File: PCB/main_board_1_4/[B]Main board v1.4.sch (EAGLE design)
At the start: 117 parts, among them J1 6P_CONN, J2 RJ11MX-95001-2661, J3 POWER_JACKPTH, J4 RJ45_MX-95001-2881, J5 RJ45_MX-95001-2881, J6 RJ45_MX-95001-2881, J7 10104111-0001LF, K1 RELAY, K2 RELAY, Q1 BC807-40SMD, T3 IRLML2244, T4 2N7002PW, U4 VREG_MIC5216, U5 TPS62133RGTT, U6 CC2D23-CHIPCAP2, U7 PIC24FJ256GB206, U8 LMC555

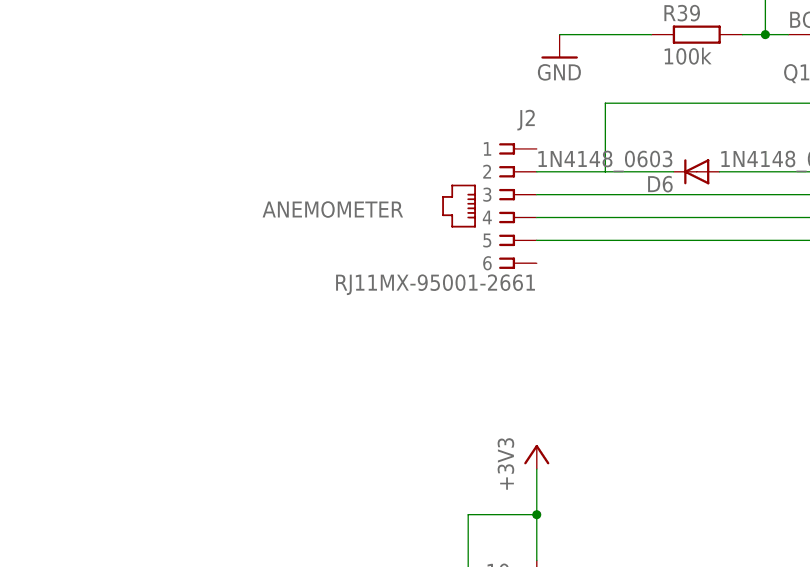
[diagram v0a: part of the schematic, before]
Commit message: Latest revision of PCB with support for RainGauge and some other sensors.
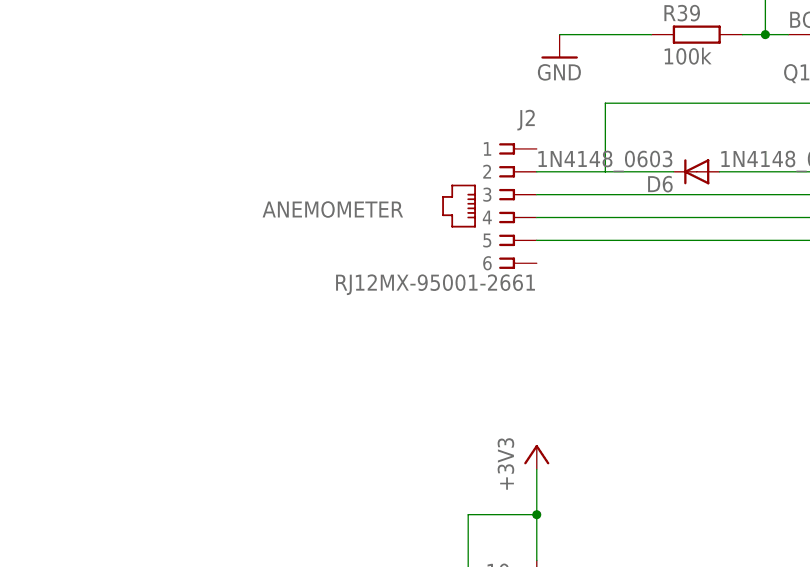
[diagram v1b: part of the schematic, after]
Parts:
- J2: value RJ11MX-95001-2661 -> RJ12MX-95001-2661; device Thomas Egnal Library:RJ11MX-95001-2661 -> Thomas Egnal Library:RJ12MX-95001-2661
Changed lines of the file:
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@@
 <part name="GND23" library="supply1" deviceset="GND" device=""/>
 <part name="C5" library="Thomas Egnal Library" deviceset="CPOL-EU" device="E2-5" value="100uF/25V"/>
-<part name="J2" library="Thomas Egnal Library" deviceset="RJ11" device="MX-95001-2661"/>
 <part name="C14" library="rcl" deviceset="C-EU" device="C1206" value="100n"/>
 <part name="GND24" library="supply1" deviceset="GND" device=""/>
@@
 <part name="R45" library="rcl" deviceset="R-EU_" device="R1206" value="1k"/>
 <part name="GND31" library="supply1" deviceset="GND" device=""/>
+<part name="J2" library="Thomas Egnal Library" deviceset="RJ12" device="MX-95001-2661"/>
 </parts>
 <sheets>
@@
 <instance part="GND23" gate="1" x="33.02" y="76.2"/>
 <instance part="C5" gate="G$1" x="-10.16" y="86.36"/>
-<instance part="J2" gate="G$1" x="-40.64" y="40.64" rot="MR0"/>
 <instance part="C14" gate="G$1" x="177.8" y="132.08" rot="R270"/>
 <instance part="GND24" gate="1" x="203.2" y="106.68"/>
@@
 </instance>
 <instance part="GND31" gate="1" x="360.68" y="-76.2"/>
+<instance part="J2" gate="G$1" x="-40.64" y="40.64" rot="MR0"/>
 </instances>
 <busses>
@@
 <net name="N$15" class="0">
 <segment>
-<pinref part="J2" gate="G$1" pin="2"/>
 <pinref part="D6" gate="G$1" pin="C"/>
 <wire x1="-38.1" y1="43.18" x2="-30.48" y2="43.18" width="0.1524" layer="91"/>
@@
 <pinref part="Q1" gate="G$1" pin="B"/>
 <wire x1="-5.08" y1="50.8" x2="-5.08" y2="53.34" width="0.1524" layer="91"/>
-</segment>
-</net>
+<pinref part="J2" gate="G$1" pin="2"/>
+</segment>
+</net>
